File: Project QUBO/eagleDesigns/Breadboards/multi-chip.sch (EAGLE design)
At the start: 15 parts, among them U1 PCA9685

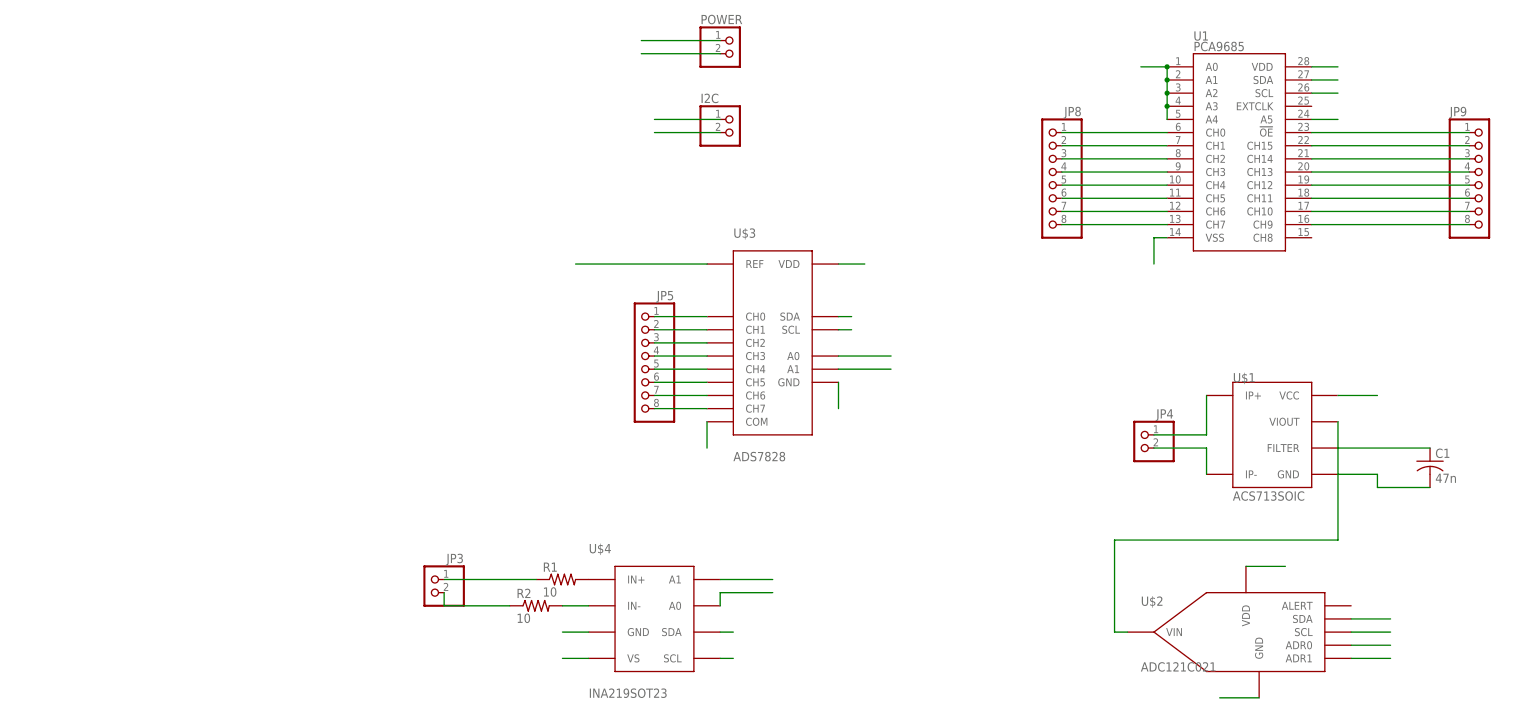
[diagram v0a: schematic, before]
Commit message: 
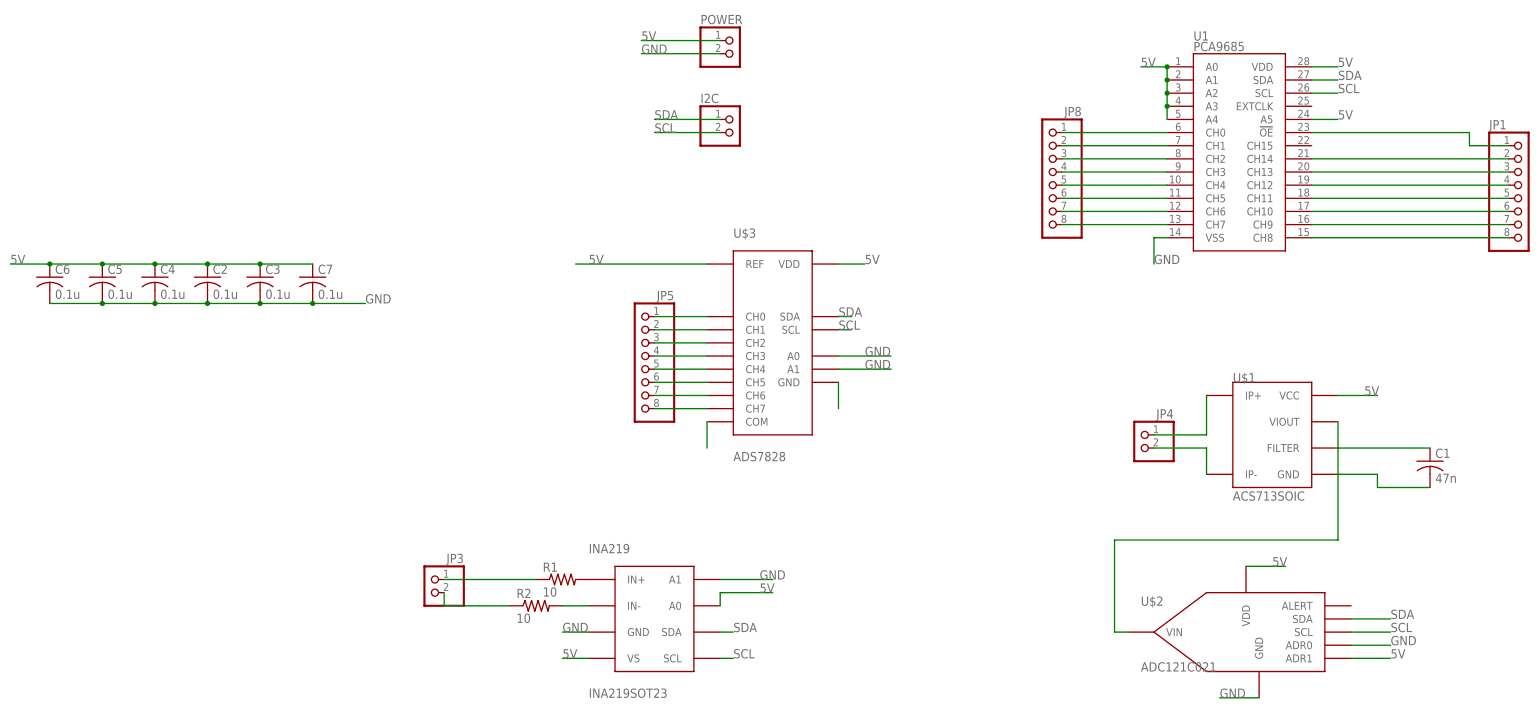
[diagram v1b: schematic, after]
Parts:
- removed JP9: (no value), pinhead:PINHD-1X8
- added C2, C3, C4, C5, C6, C7: 0.1u, resistor:C-USC0805
- added JP1: (no value), pinhead:PINHD-1X8
- renumbered U$4 to INA219
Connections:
- removed net N$59: JP9.2, U1.CH15
- new net N$4: JP1.8, U1.CH8
- net 5V: now also C2.1, C3.1, C4.1, C5.1, C6.1, C7.1
- net GND: now also C2.2, C3.2, C4.2, C5.2, C6.2, C7.2
- net N$58: now also JP1.1; no longer JP9.1
- net N$60: now also JP1.2; no longer JP9.3
- net N$61: now also JP1.3; no longer JP9.4
- net N$62: now also JP1.4; no longer JP9.5
- net N$63: now also JP1.5; no longer JP9.6
- net N$64: now also JP1.6; no longer JP9.7
- net N$65: now also JP1.7; no longer JP9.8
